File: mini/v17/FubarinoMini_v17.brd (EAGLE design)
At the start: 50.8 x 17.8 mm, 38 parts, among them IC1 AZ1117CR2-3.3TRG1, J1 M20, J2 M20, J8 USB-5PIN, Q1 8MHz, Q2 32.768 KHz, U1 PIC32MX270F256D_44QFN_44

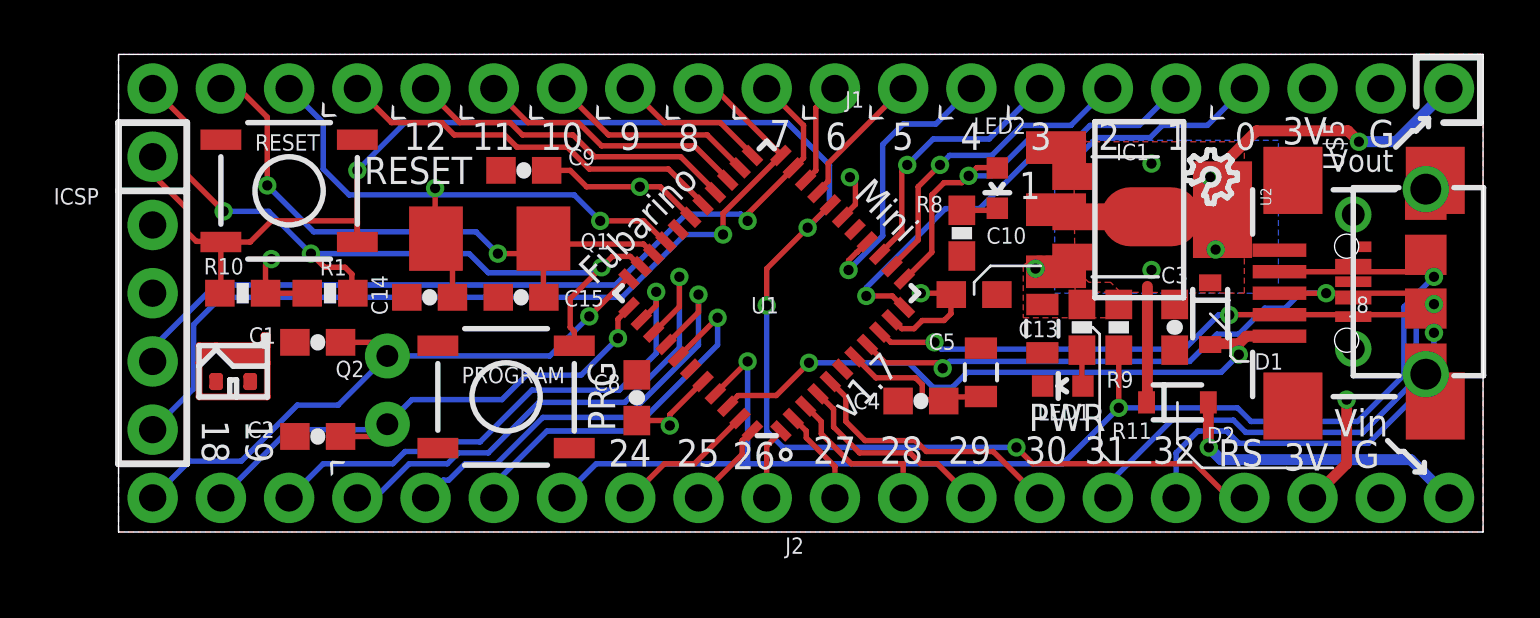
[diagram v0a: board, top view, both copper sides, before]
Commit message: Version 2.0, first draft, done and sent to PCB fab. Changed switches, crystal, USB connector, rerouted most of board. Still need to rename folder to 2.0
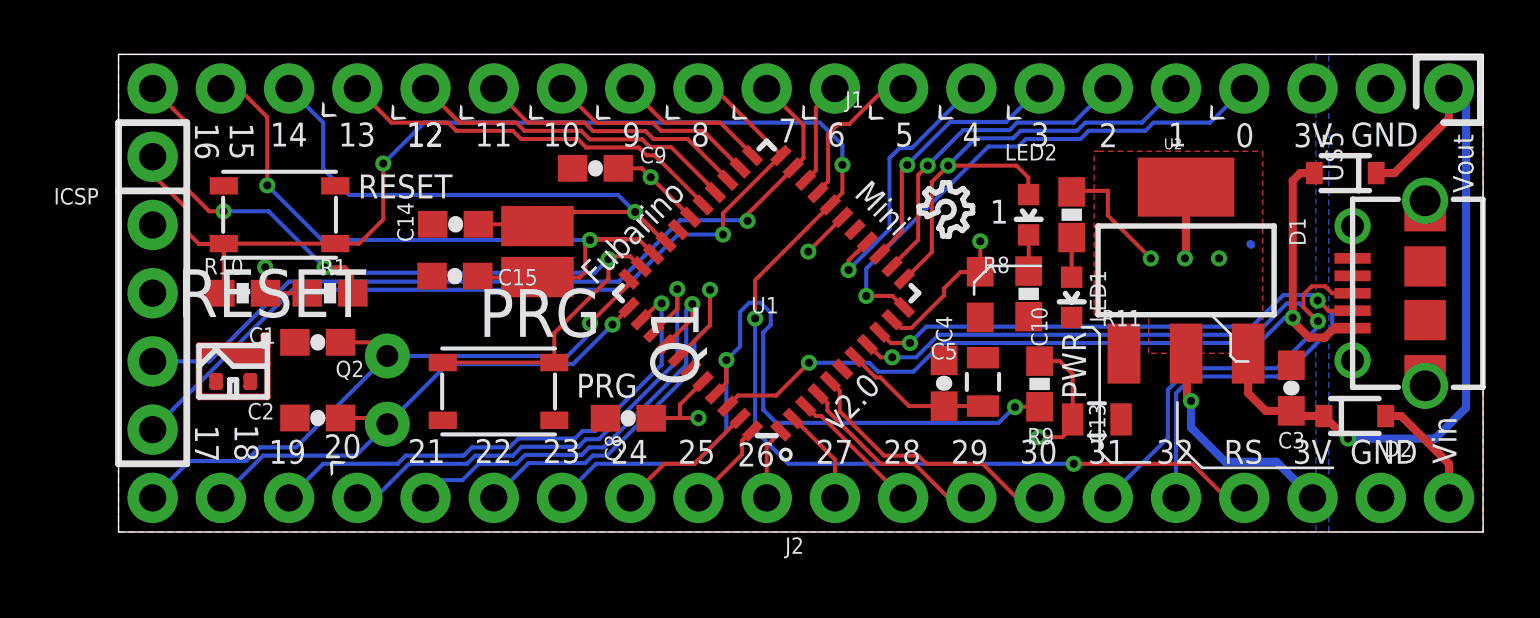
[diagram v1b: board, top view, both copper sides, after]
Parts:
- removed IC1: AZ1117CR2-3.3TRG1, linear:SOT89
- removed J8: USB-5PIN, SchmalzHaus:USB-MINIB-5PIN-HIROSE-UX60-MB-5ST
- removed PROGRAM: (no value), SparkFun02-20-08:TACTILE_SWITCH_SMD
- added PRG: PTS_810, CK_PTS_810_TactSwitch:PTS_810
- C3: value 1uF -> 4.7uF >25V
- Q1: device SchmalzHaus:NX5032_5MM_3.2MM_CRYSTAL -> NDK_NX3225GD_Crystal:NX3225GD
- RESET: value (none) -> PTS_810; device SparkFun02-20-08:TACTILE_SWITCH_SMD -> CK_PTS_810_TactSwitch:PTS_810
- U2: value (none) -> SPX1117M3-L-3-3/TR
- moved LOGO1 9.93 mm to (29.6, 12.2)
- moved D1 7.26 mm to (45.7, 13.4), turned to 180 degrees
- moved D2 6.62 mm to (46.0, 4.32)
- moved C3 4.90 mm to (43.7, 5.36), turned to 90 degrees
- moved R11 4.21 mm to (35.5, 11.8)
- moved C13 3.94 mm to (36.4, 4.19), turned to 0 degrees
- moved R9 3.62 mm to (34.3, 5.51)
- moved R8 3.36 mm to (33.9, 8.86)
- moved LED1 3.32 mm to (35.5, 8.74), turned to 180 degrees
- moved C14 2.88 mm to (12.5, 11.5)
- moved U2 2.85 mm to (39.7, 9.74), turned to 0 degrees
- moved C9 2.67 mm to (17.8, 13.5)
- moved C15 2.59 mm to (12.5, 9.53)
- moved Q1 1.84 mm to (15.6, 10.4), turned to 90 degrees
- moved LED2 1.53 mm to (33.9, 11.8)
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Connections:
- net !MCLR!: now also RESET.P$3, RESET.P$4; no longer RESET.3, RESET.4
- net 3.3V: now also U2.2, U2.4; no longer IC1.3
- net 5V: now also U2.3; no longer IC1.2, IC1.2@1
- net D+/RB10: now also U$5.D+; no longer J8.D+
- net D-/RB11: now also U$5.D-; no longer J8.D-
- net GND: now also PRG.P$1, PRG.P$2, RESET.P$1, RESET.P$2, U$5.GND, U$5.GND@1, U$5.GND@2, U$5.GND@3, U$5.GND@4, U$5.GND@5, U$5.GND@6, U$5.GND@7, U$5.GND@8, U2.1; no longer IC1.1, J8.GND, J8.MTN1, J8.MTN2, J8.MTN3, J8.MTN4, PROGRAM.1, PROGRAM.2, RESET.1, RESET.2
- net RA2: now also Q1.P$1; no longer Q1.1
- net RA3: now also Q1.P$2; no longer Q1.2
- net RA8: now also PRG.P$3, PRG.P$4; no longer PROGRAM.3
- net USBID/RB5: no longer J8.ID
- net VBUS: now also U$5.VBUS; no longer J8.VBUS
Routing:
- net USBID/RB5: track 51.3 -> 29.1 mm, vias 3 -> 2
- net 3.3V: track 22.9 -> 37.7 mm, vias 7 -> 10
- net 5V: track 15.0 -> 27.6 mm, vias 5 -> 1
- net D+/RB10: track 41.6 -> 33.1 mm, vias 3 -> 2
- net VBUS: track 23.7 -> 31.5 mm
- net VIN: track 11.4 -> 4.36 mm, vias 1 -> 0
- net D-/RB11: track 36.6 -> 30.7 mm, vias 3 -> 2
- net RA8: track 28.6 -> 33.6 mm
- net RA3: track 22.9 -> 27.0 mm
- net RA10: track 15.5 -> 18.4 mm
- net RC5: track 14.1 -> 15.6 mm
- net RA2: track 22.1 -> 23.5 mm, vias 2 -> 1
- net RB1: track 33.6 -> 32.2 mm
- net RC7: track 6.06 -> 5.04 mm
- net !MCLR!: track 65.4 -> 64.5 mm
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- added copper zone on layer 16, net GND
- removed copper zone on layer 1, net 5V
- removed copper zone on layer 16, net 5V
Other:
- board text added: "13"
- board text added: "20"
- board text added: "v2.0"
- board text removed: "G"
- board text removed: "v1.7"

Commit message: Minor silk screen adjustments for readability, and moving a couple caps around for easier assembly.
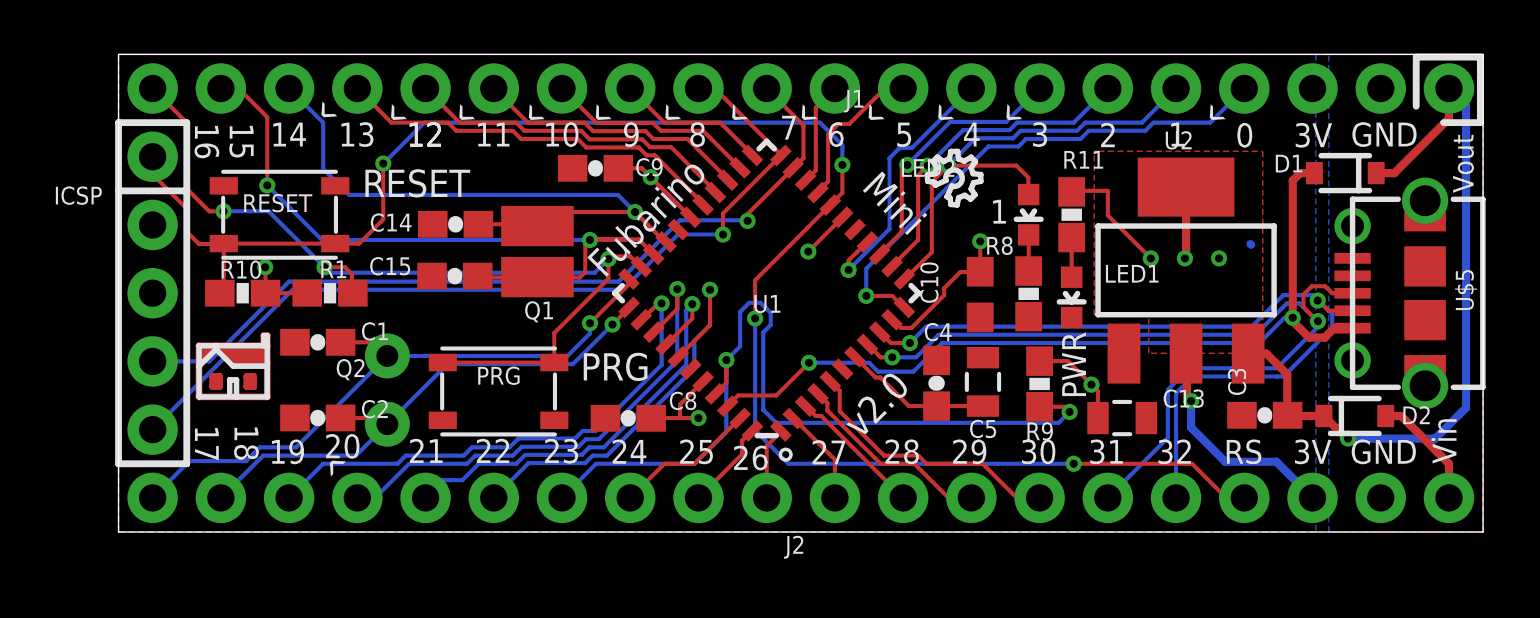
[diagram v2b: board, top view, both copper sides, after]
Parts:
- moved C3 1.42 mm to (42.7, 4.34), turned to 180 degrees
- moved LOGO1 1.21 mm to (29.9, 13.3)
- moved C13 0.94 mm to (37.4, 4.24)
- moved C4 0.28 mm to (30.5, 5.54)
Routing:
- net USBID/RB5: track 29.1 -> 31.4 mm
- net 3.3V: track 37.7 -> 36.2 mm
